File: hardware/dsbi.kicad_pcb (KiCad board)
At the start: 2 copper layers, 20 parts, among them U1 TL082, U2 TL082

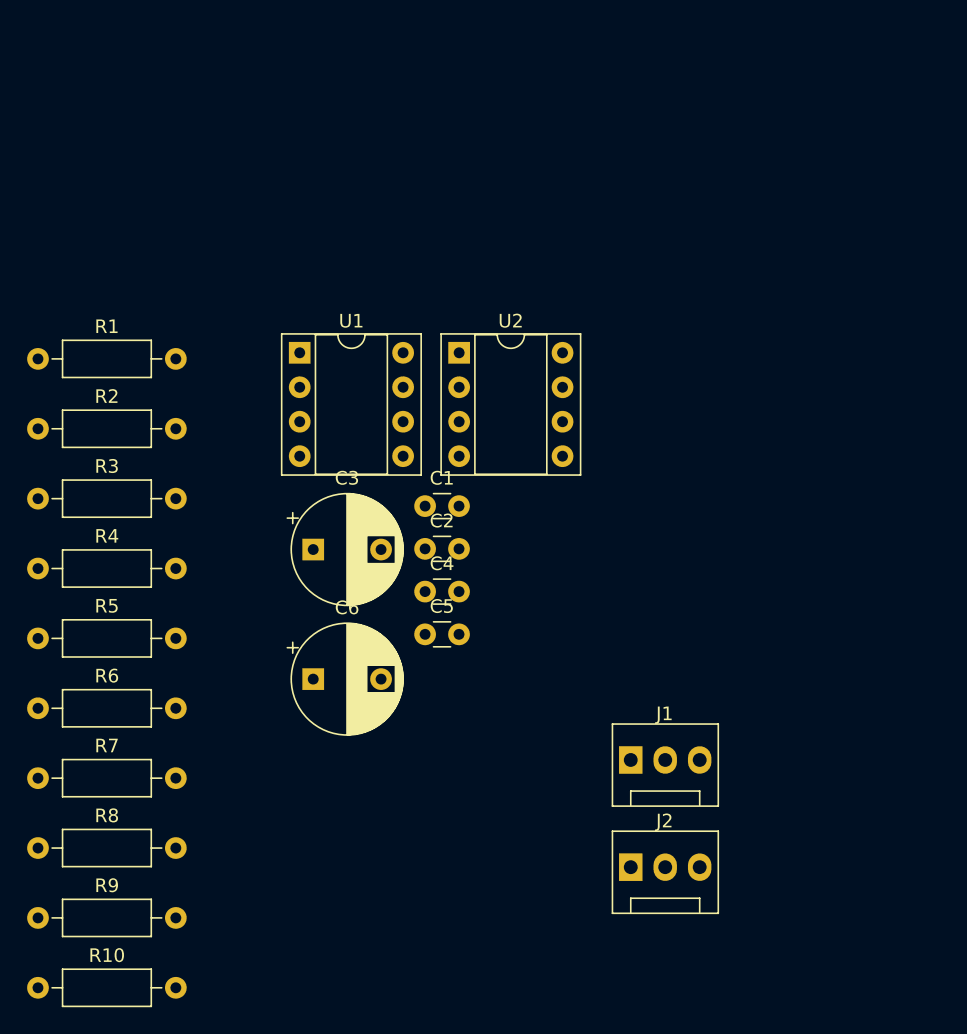
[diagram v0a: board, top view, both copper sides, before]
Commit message: Arrangement of elements
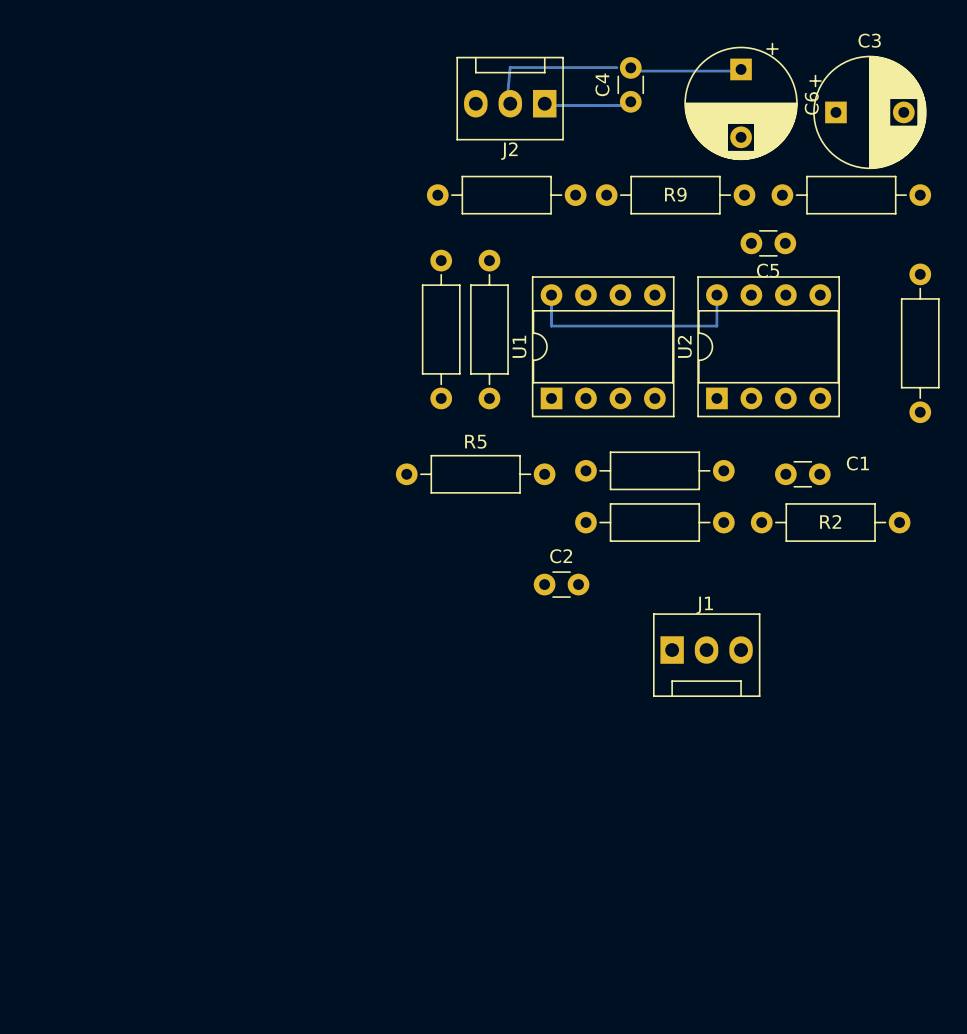
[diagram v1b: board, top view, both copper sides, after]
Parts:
- moved R10 80.1 mm to (128.0, 49.3)
- moved R9 67.8 mm to (115.1, 49.3)
- moved R1 65.1 mm to (138.2, 65.3), turned to 90 degrees
- moved R2 63.9 mm to (136.7, 73.4), turned to 180 degrees
- moved J2 56.6 mm to (110.5, 42.5), turned to 180 degrees
- moved R8 56.4 mm to (102.6, 49.3)
- moved C6 54.9 mm to (125.0, 40.0), turned to -90 degrees
- moved R4 50.7 mm to (123.7, 73.4), turned to 180 degrees
- moved R3 50.6 mm to (123.7, 69.6), turned to 180 degrees
- moved C3 50.2 mm to (132.0, 43.2)
- moved R7 43.5 mm to (106.4, 64.3), turned to 90 degrees
- moved C5 39.2 mm to (128.2, 52.8), turned to 180 degrees
- moved C4 39.2 mm to (116.8, 42.4), turned to 90 degrees
- moved R6 37.5 mm to (102.9, 64.3), turned to 90 degrees
- moved R5 29.7 mm to (100.3, 69.8)
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
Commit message: paths
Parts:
- moved R1 14.8 mm to (137.2, 80.0), turned to 180 degrees
- moved R6 12.1 mm to (105.9, 52.6), turned to 0 degrees
- moved R7 8.65 mm to (105.9, 55.6), turned to 0 degrees
- moved R10 8.64 mm to (135.9, 52.8), turned to 180 degrees
- moved R5 5.95 mm to (105.9, 71.9), turned to 90 degrees
- moved C3 3.64 mm to (130.4, 46.5)
- moved J1 3.31 mm to (116.6, 83.1)
- moved C5 3.05 mm to (128.2, 55.9)
- moved R2 2.59 mm to (137.2, 75.9)
- moved C1 2.54 mm to (130.8, 72.4)
- moved C2 2.54 mm to (110.5, 80.5)
- moved U1 2.54 mm to (111.0, 66.8)
- moved U2 2.54 mm to (123.2, 66.8)
- moved R4 2.54 mm to (123.7, 75.9)
- moved R3 2.29 mm to (123.7, 71.9)

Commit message: Most paths
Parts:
- added J1: ~, Connector:FanPinHeader_1x03_P2.54mm_Vertical, F.Cu at (67.1, 56.6)
- added J2: ~, Connector:FanPinHeader_1x03_P2.54mm_Vertical, F.Cu at (61.2, 19.7)
- moved R2 97.4 mm to (42.9, 51.3)
- moved R4 96.7 mm to (30.2, 51.3)
- moved C2 94.7 mm to (19.3, 55.1)
- moved R1 94.3 mm to (46.2, 54.9)
- moved C6 93.9 mm to (34.0, 16.6)
- moved C4 93.1 mm to (26.7, 19.3)
- moved J1 93.1 mm to (27.4, 56.4)
- moved R10 92.8 mm to (46.0, 29.7)
- moved R3 92.7 mm to (34.3, 47.5)
- moved C3 92.7 mm to (40.8, 23.1)
- moved C1 92.3 mm to (41.9, 47.5)
- moved J2 91.9 mm to (21.6, 19.4)
- moved R5 91.9 mm to (17.0, 48.8)
- moved R6 91.9 mm to (17.0, 29.5)
- moved R7 91.9 mm to (17.0, 32.5)
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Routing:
- net (no net): vias 0 -> 4
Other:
- board outline added: 73.7 x 46.5 mm

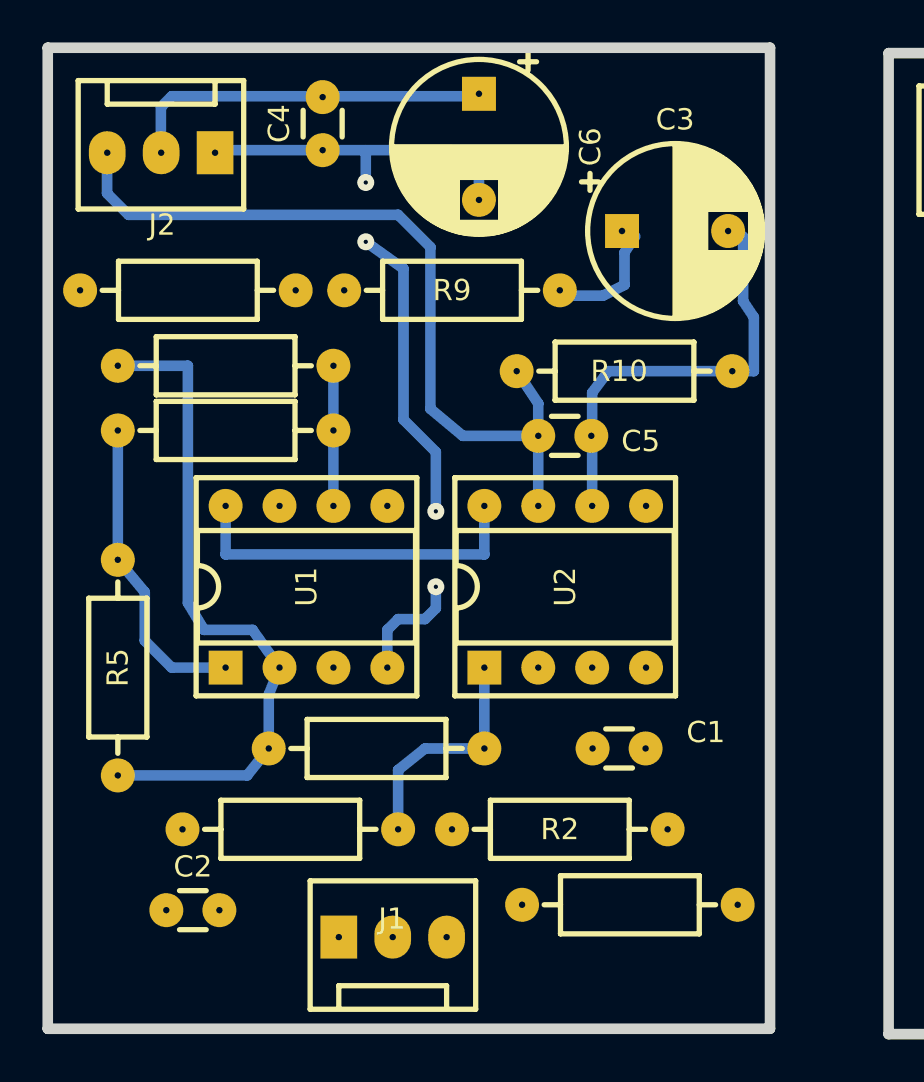
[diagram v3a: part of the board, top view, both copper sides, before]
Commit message: Rearrange elements
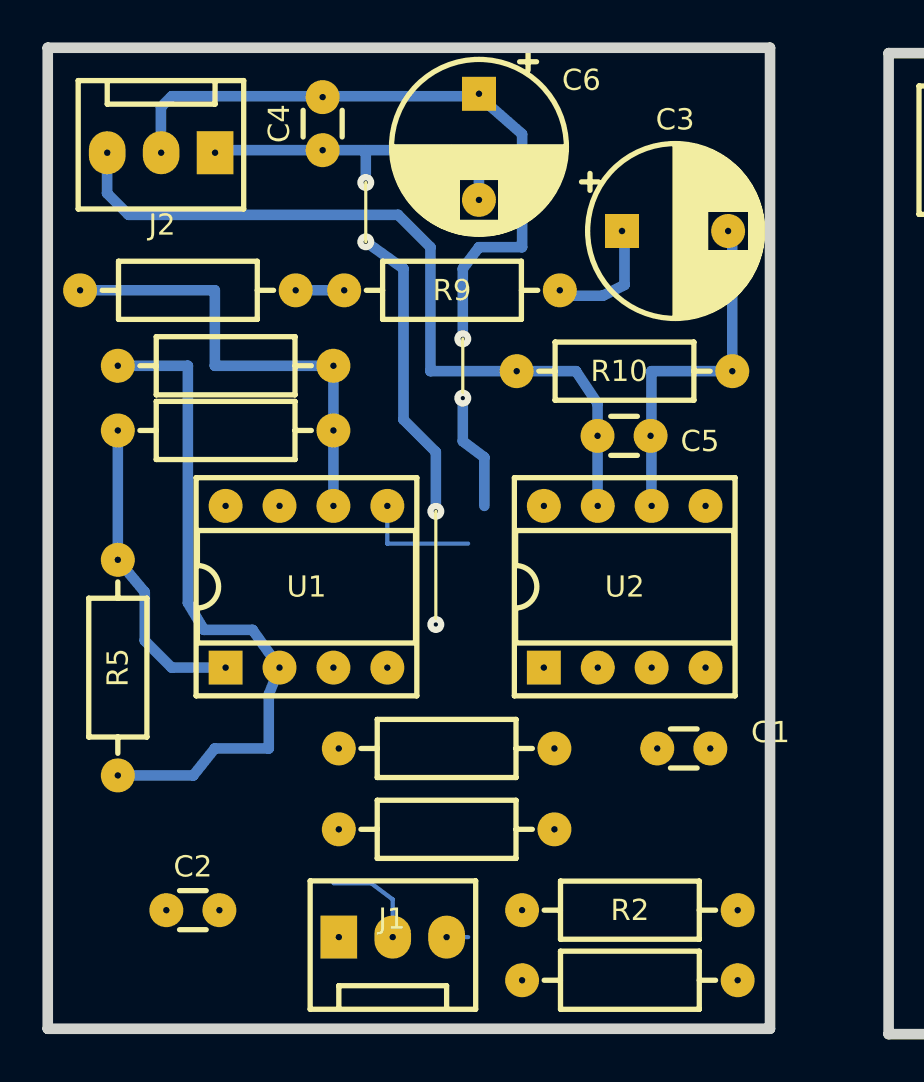
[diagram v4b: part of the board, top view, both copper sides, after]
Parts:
- moved R8 10.2 mm to (15.2, 25.9), turned to 0 degrees
- moved R4 7.37 mm to (37.6, 51.3)
- moved R2 5.04 mm to (46.2, 55.1)
- moved R1 3.56 mm to (46.2, 58.4)
- moved R3 3.30 mm to (37.6, 47.5)
- moved C1 3.05 mm to (44.9, 47.5)
- moved U2 2.80 mm to (37.1, 43.7)
- moved C5 2.79 mm to (42.1, 32.8)
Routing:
- net (no net): vias 4 -> 6

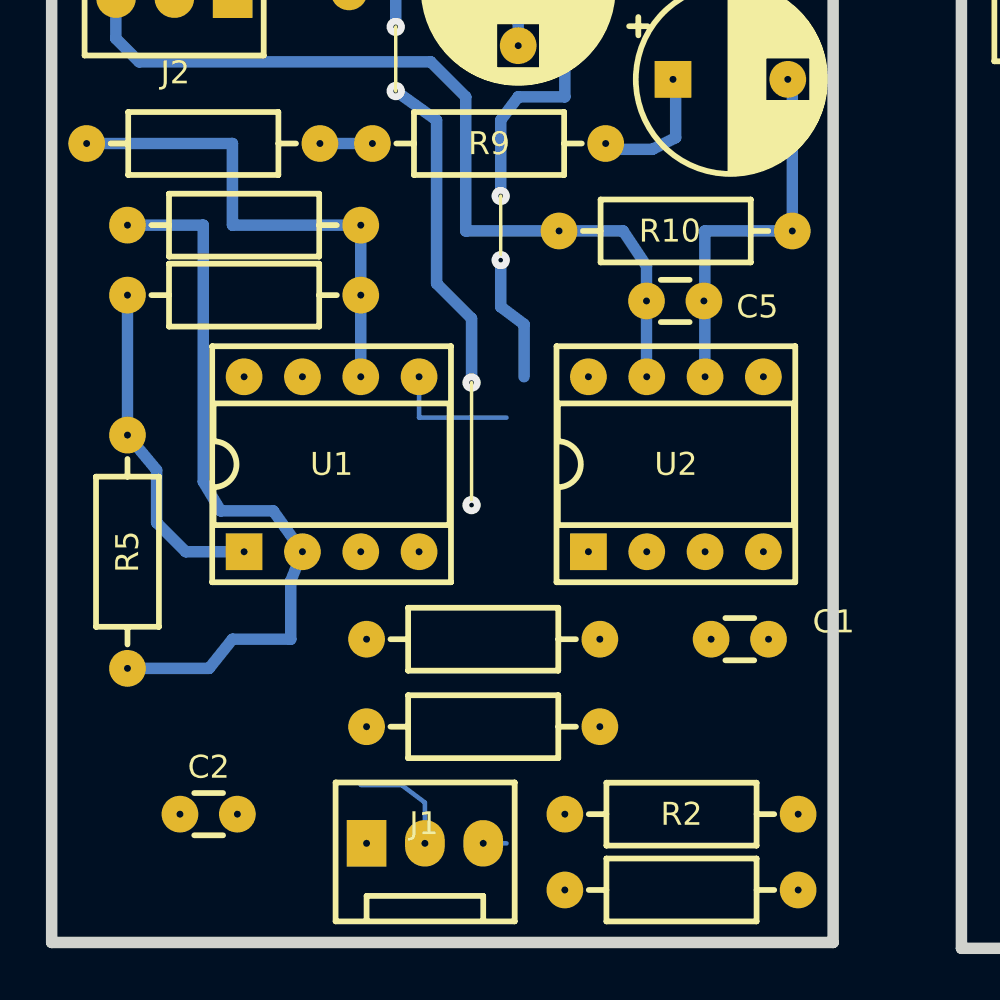
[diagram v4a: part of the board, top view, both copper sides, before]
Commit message: Create new PCB paths
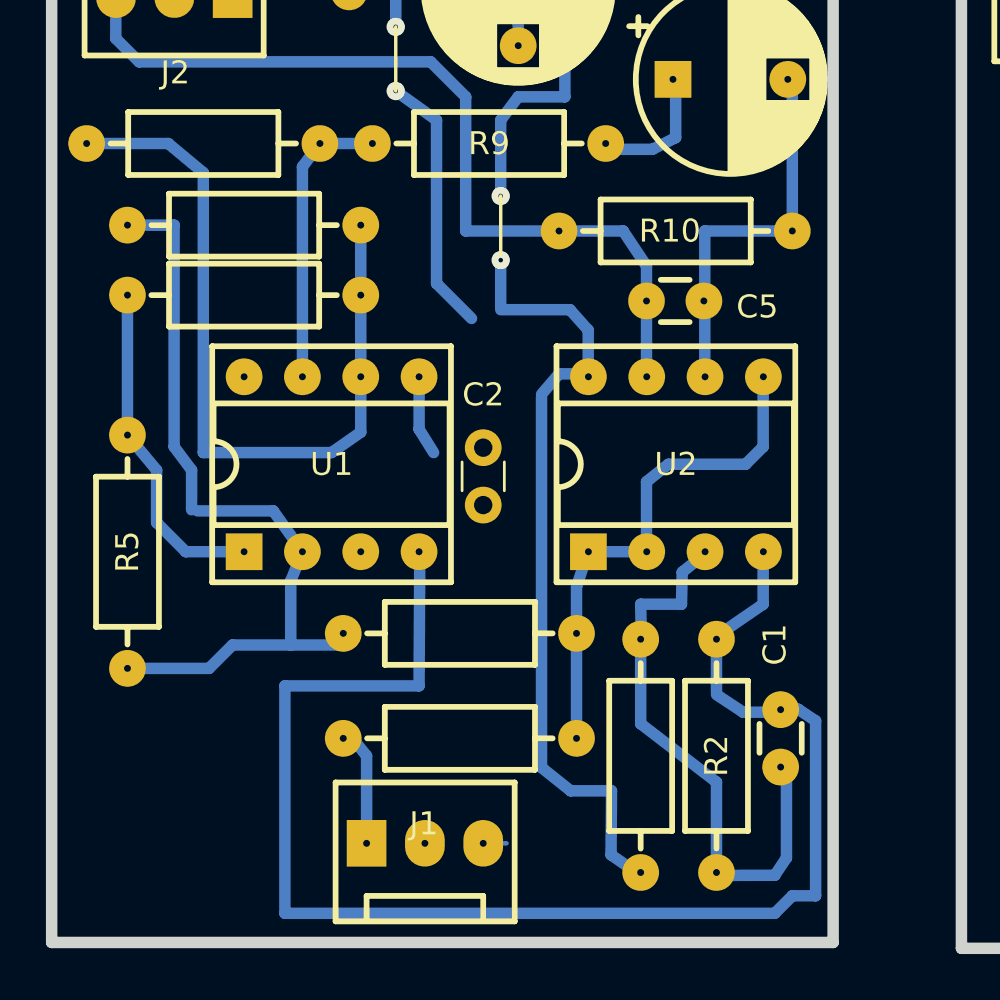
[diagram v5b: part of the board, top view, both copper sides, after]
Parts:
- moved C2 18.9 mm to (32.5, 41.7), turned to 90 degrees
- moved R1 12.9 mm to (39.4, 47.5), turned to -90 degrees
- moved R2 8.41 mm to (42.7, 47.5), turned to -90 degrees
- moved C1 3.11 mm to (45.5, 50.6), turned to -90 degrees
- moved R4 1.14 mm to (36.6, 51.8)
- moved R3 1.05 mm to (36.6, 47.2)
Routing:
- net (no net): vias 6 -> 4

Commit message: Finish analog part
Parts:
- removed the J1 at (67.1, 56.6)
- removed the J2 at (61.2, 19.7)
- moved C1 2.53 mm to (44.1, 48.5)
- moved C3 2.53 mm to (39.4, 21.0)
- moved J2 2.53 mm to (20.2, 17.3)
- moved R3 2.53 mm to (35.2, 45.1)
- moved R4 2.53 mm to (35.2, 49.7)
- moved U2 2.53 mm to (35.7, 41.6)
- moved R5 2.53 mm to (15.6, 46.7)
- moved C6 2.53 mm to (32.6, 14.5)
- moved J1 2.53 mm to (26.0, 54.3)
- moved U1 2.53 mm to (20.7, 41.6)
- moved C4 2.53 mm to (25.3, 17.2)
- moved C5 2.53 mm to (40.7, 30.7)
- moved R1 2.53 mm to (38.0, 45.4)
- moved R10 2.53 mm to (44.6, 27.6)
- moved R2 2.53 mm to (41.3, 45.4)
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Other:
- board size 73.7 x 46.5 mm -> 34 x 46.2 mm
- board text added: "Damn Simple Brainwave Interface (Amplifier) rev 1.0"

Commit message: fix details
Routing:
- net (no net): vias 4 -> 6
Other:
- board outline removed
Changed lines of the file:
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@@
     (thickness 1.6)
   )
-  (paper "A4")
+  (paper "A5" portrait)
   (layers
     (0 "F.Cu" signal)
@@
     (pad_to_mask_clearance 0)
     (pcbplotparams
-      (layerselection 0x0001020_fffffffe)
-      (plot_on_all_layers_selection 0x0001000_00000000)
+      (layerselection 0x0000020_7ffffffe)
+      (plot_on_all_layers_selection 0x0000000_00000001)
       (disableapertmacros false)
       (usegerberextensions false)
@@
       (plotvalue true)
       (plotinvisibletext false)
-      (sketchpadsonfab false)
+      (sketchpadsonfab true)
       (subtractmaskfromsilk false)
       (outputformat 4)
       (mirror true)
-      (drillshape 0)
+      (drillshape 2)
       (scaleselection 1)
-      (outputdirectory "amp-mirror")
+      (outputdirectory "")
     )
   )
@@
   (gr_line (start 31.887465 28.620508) (end 31.887465 26.588508)
     (stroke (width 0.15) (type default)) (layer "F.SilkS"))
-  (gr_rect (start 12.329465 12.364508) (end 46.365465 58.592508)
-    (stroke (width 0.1) (type default)) (fill none) (layer "Edge.Cuts"))
   (gr_text "Damn\nSimple\nBrainwave\nInterface\n(Amplifier)\nrev 1.0" (at 21.290192 55.768032) (layer "B.Cu")
     (effects (font (size 0.8 0.8) (thickness 0.2) bold) (justify left bottom mirror))
@@
   (via (at 30.109465 21.762508) (size 0.8) (drill 0.2) (layers "F.Cu" "B.Cu") (net 0))
   (via (at 31.887465 28.874508) (size 0.8) (drill 0.2) (layers "F.Cu" "B.Cu") (net 0))
+  (via (at 45.593 13.081) (size 1) (drill 0.5) (layers "F.Cu" "B.Cu") (net 0))
   (via (at 31.887465 26.455008) (size 0.8) (drill 0.2) (layers "F.Cu" "B.Cu") (net 0))
+  (via (at 13.208 57.658) (size 1) (drill 0.5) (layers "F.Cu" "B.Cu") (net 0))
 )
